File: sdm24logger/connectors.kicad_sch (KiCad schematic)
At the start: 23 parts, among them J3 USB_B, J4 1-776087-4, J5 1-776087-1, U10 SN65HVD230, U11 TLX9291A, U12 TCA9406DC, U13 ADC128D818, U8 USBLC6-2SC6, U9 SN65HVD230

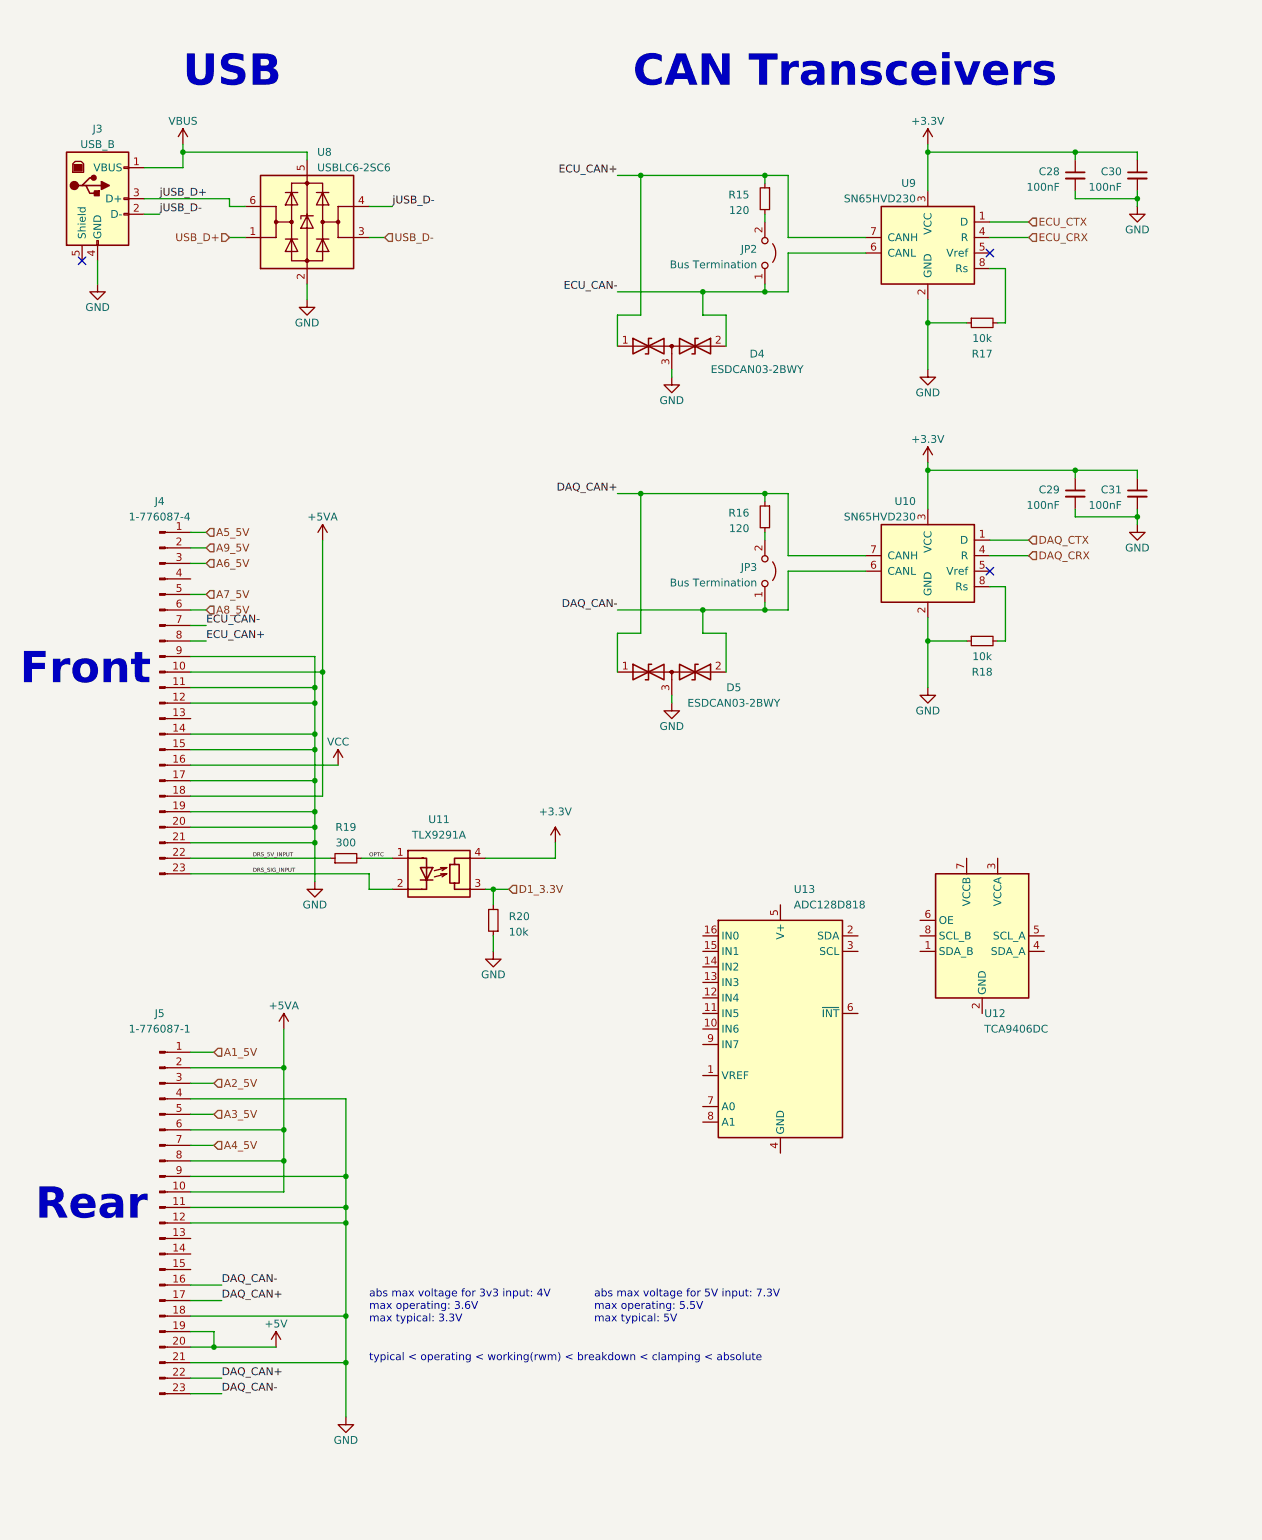
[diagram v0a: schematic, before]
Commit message: adding model for i2c shifter
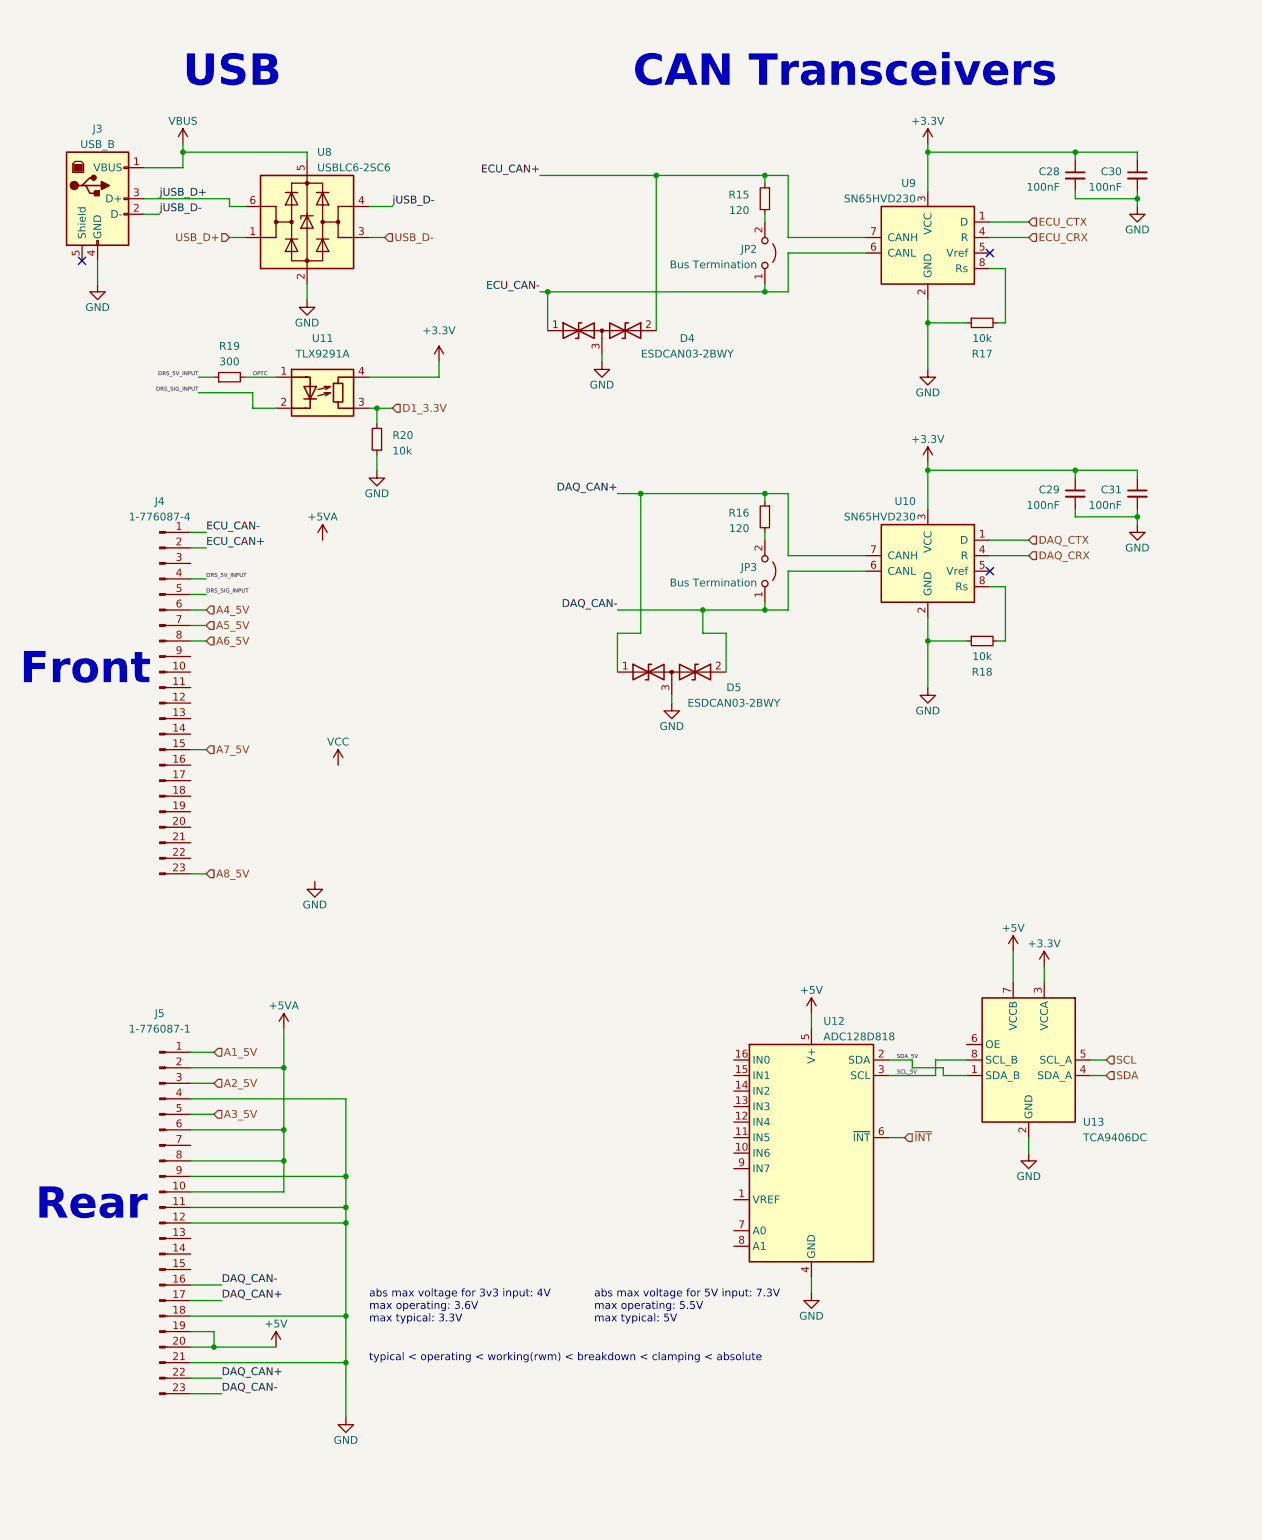
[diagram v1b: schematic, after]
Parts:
- U13: renamed from U12; footprint (none) -> Library:TI_SSOP_8_2.9x4.25x0.65
- renumbered U13 to U12
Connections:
- net A9_5V is gone; now on net ECU_CAN+: J4.2 (Pin_2)
- net +3.3V: now also U13.3 (VCCA)
- net +5V: now also U12.5 (V+), U13.7 (VCCB)
- net +5VA: no longer J4.10 (Pin_10), J4.18 (Pin_18)
- net A4_5V: now also J4.6 (Pin_6); no longer J5.7 (Pin_7)
- net A5_5V: now also J4.7 (Pin_7); no longer J4.1 (Pin_1)
- net A6_5V: now also J4.8 (Pin_8); no longer J4.3 (Pin_3)
- net A7_5V: now also J4.15 (Pin_15); no longer J4.5 (Pin_5)
- net A8_5V: now also J4.23 (Pin_23); no longer J4.6 (Pin_6)
- net DRS_5V_INPUT: now also J4.4 (Pin_4); no longer J4.22 (Pin_22)
- net DRS_SIG_INPUT: now also J4.5 (Pin_5); no longer J4.23 (Pin_23)
- net ECU_CAN+: now also D4.2 (A2); no longer D4.1 (A1), J4.8 (Pin_8)
- net ECU_CAN-: now also D4.1 (A1), J4.1 (Pin_1); no longer D4.2 (A2), J4.7 (Pin_7)
- net GND: now also U12.4 (GND), U13.2 (GND); no longer J4.11 (Pin_11), J4.12 (Pin_12), J4.14 (Pin_14), J4.15 (Pin_15), J4.17 (Pin_17), J4.19 (Pin_19), J4.20 (Pin_20), J4.21 (Pin_21), J4.9 (Pin_9)
- net VCC: no longer J4.16 (Pin_16)
- net SDA_5V: now reaches U13.1 (SDA_B)
- net SDA_5V: now also U12.2 (SDA)
- net SDA: now reaches U13.4 (SDA_A)
- net SCL: now reaches U13.5 (SCL_A)
- net SCL_5V: now reaches U13.8 (SCL_B)
- net SCL_5V: now also U12.3 (SCL)
- net ~{INT}: now reaches U12.6 (~{INT})
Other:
- moved on the sheet: D4, R19, R20, U11, U12, U13

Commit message: uploading
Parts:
- added C34, C35: 100nF, Capacitor_SMD:C_0402_1005Metric, symbol Device:C_Small
- added R21: 10k, Resistor_SMD:R_0603_1608Metric, symbol Device:R_Small
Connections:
- net +3.3V: now also C35.1
- net +5V: now also C34.1
- net +5VA: no longer J5.8 (Pin_8)
- net DAQ_CAN+: now also J5.7 (Pin_7); no longer J5.17 (Pin_17)
- net DAQ_CAN-: now also J5.8 (Pin_8); no longer J5.16 (Pin_16)
- net GND: now also C34.2, C35.2, R21.1; no longer J5.9 (Pin_9)
- net OE: now reaches U13.6 (OE)
- net OE: now also R21.2
- net A1_5V: no longer names the net of J5.1 (Pin_1)
- net A2_5V: no longer names the net of J5.3 (Pin_3)
- net A3_5V: no longer names the net of J5.5 (Pin_5)
- net A4_5V: no longer names the net of J4.6 (Pin_6)
- net A5_5V: no longer names the net of J4.7 (Pin_7)
- net A6_5V: no longer names the net of J4.8 (Pin_8)
- net A7_5V: no longer names the net of J4.15 (Pin_15)
- net A8_5V: no longer names the net of J4.23 (Pin_23)
- no-connect marks 3 -> 5
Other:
- moved on the sheet: U12

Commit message: ADC pinouts
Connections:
- net +5VA is gone; now on net +5V: J5.10 (Pin_10), J5.2 (Pin_2), J5.6 (Pin_6)
- net GND: now also U12.7 (A0), U12.8 (A1)
- net VCC: now also J4.16 (Pin_16)
- net AIN1: now reaches J4.15 (Pin_15)
- net AIN1: now also U12.12 (IN4)
- net AIN0: now reaches J4.23 (Pin_23)
- net AIN0: now also U12.13 (IN3)
- net AIN4: now reaches J4.6 (Pin_6)
- net AIN4: now also U12.9 (IN7)
- net AIN3: now reaches J4.7 (Pin_7)
- net AIN3: now also U12.10 (IN6)
- net AIN2: now reaches J4.8 (Pin_8)
- net AIN2: now also U12.11 (IN5)
- net AIN7: now reaches U12.14 (IN2)
- net AIN7: now also J5.16 (Pin_16)
- net AIN6: now reaches U12.15 (IN1)
- net AIN6: now also J5.9 (Pin_9)
- net AIN5: now reaches U12.16 (IN0)
- net AIN5: now also J5.1 (Pin_1)

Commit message: uploading changes
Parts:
- removed C34, C35: 100nF, Capacitor_SMD:C_0402_1005Metric, symbol Device:C_Small
- removed R21: 10k, Resistor_SMD:R_0603_1608Metric, symbol Device:R_Small
- removed U12: ADC128D818, Package_SO:TSSOP-16_4.4x5mm_P0.65mm, symbol Analog_ADC:ADC128D818
- removed U13: TCA9406DC, Library:TI_SSOP_8_2.9x4.25x0.65, symbol Interface:TCA9406DC
- added U12: ADR425ARMZ, Package_SO:MSOP-8_3x3mm_P0.65mm, symbol Reference_Voltage:ADR425ARMZ
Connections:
- net AIN0: now also J5.1 (Pin_1); no longer J4.23 (Pin_23)
- net AIN1: now also J5.9 (Pin_9); no longer J4.15 (Pin_15)
- net AIN2: now also J5.16 (Pin_16); no longer J4.8 (Pin_8)
- net AIN3: now also J4.23 (Pin_23); no longer J4.7 (Pin_7)
- net AIN4: now also J4.15 (Pin_15); no longer J4.6 (Pin_6)
- net AIN5: now also J4.8 (Pin_8); no longer J5.1 (Pin_1)
- net AIN6: now also J4.7 (Pin_7); no longer J5.9 (Pin_9)
- net AIN7: now also J4.6 (Pin_6); no longer J5.16 (Pin_16)
- net GND: now also U12.4 (GND)
- net VCC: now also U12.2 (VIN)
- new net +5VA: U12.6 (OUT)
- no-connect marks 5 -> 6

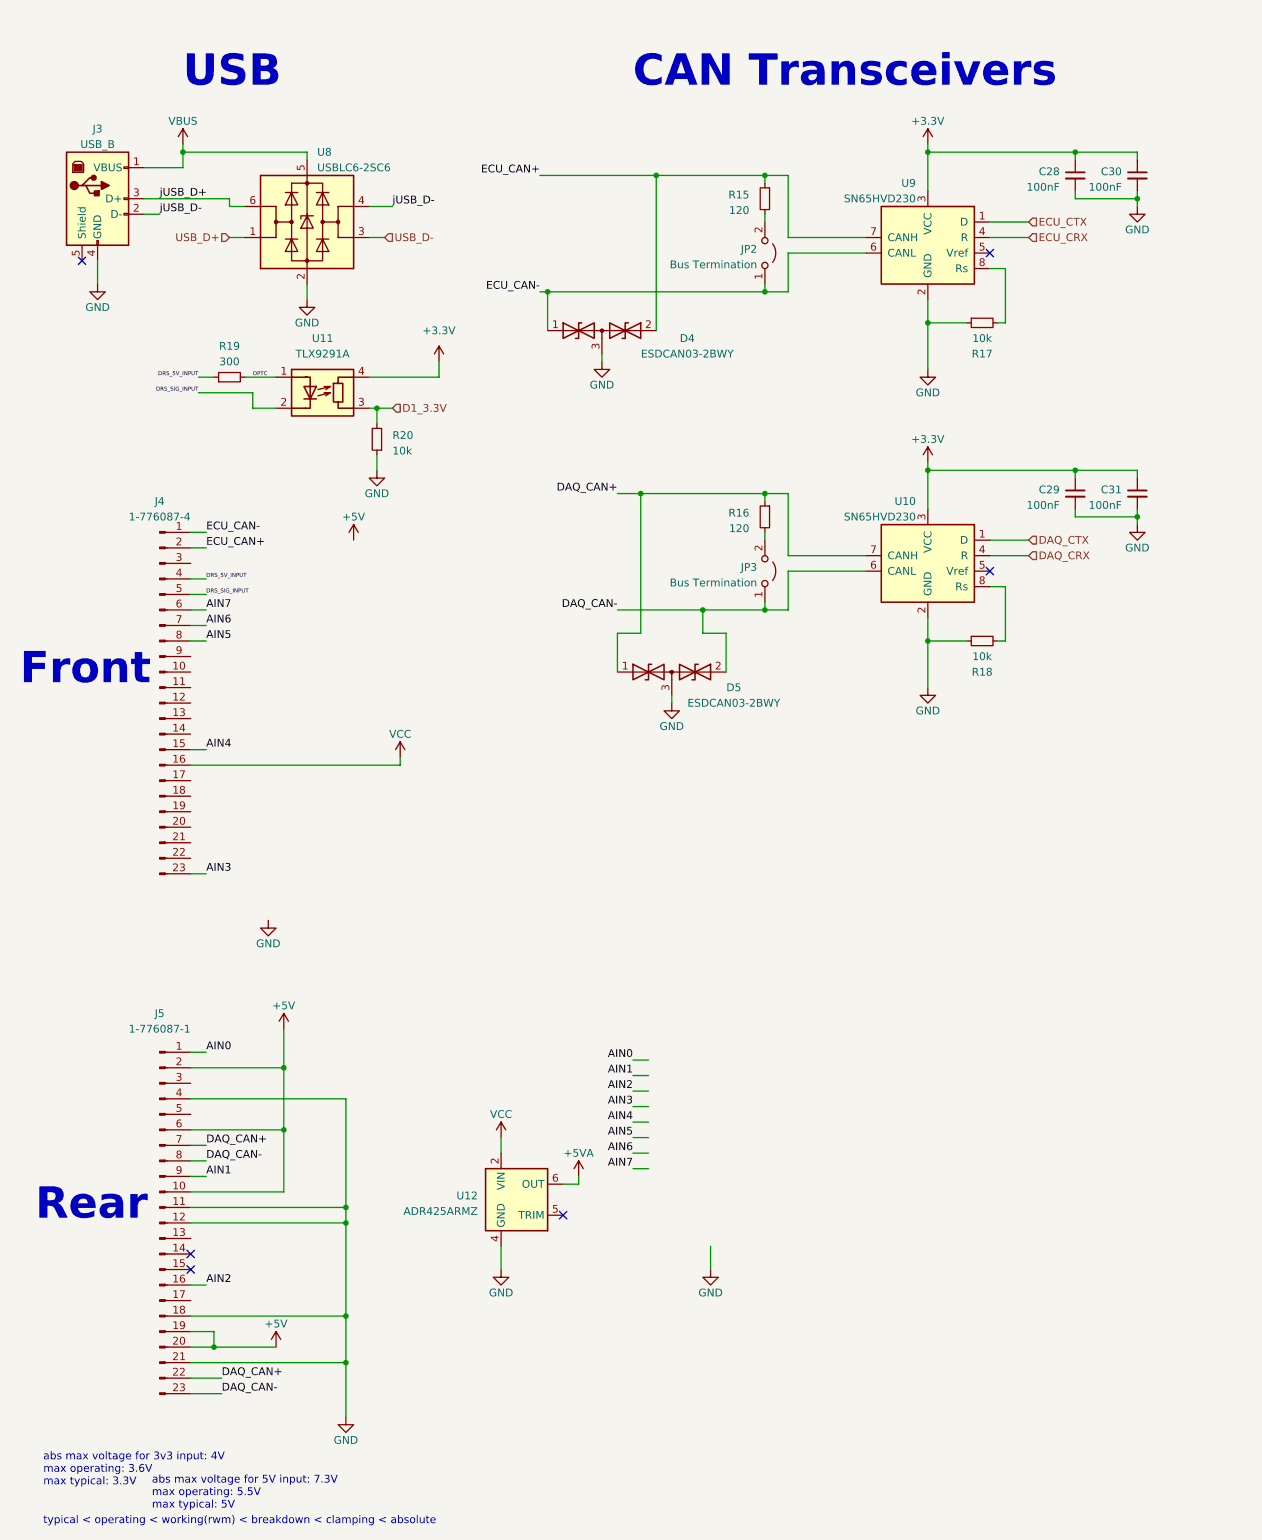
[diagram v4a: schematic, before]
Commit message: add footprints for volt ref
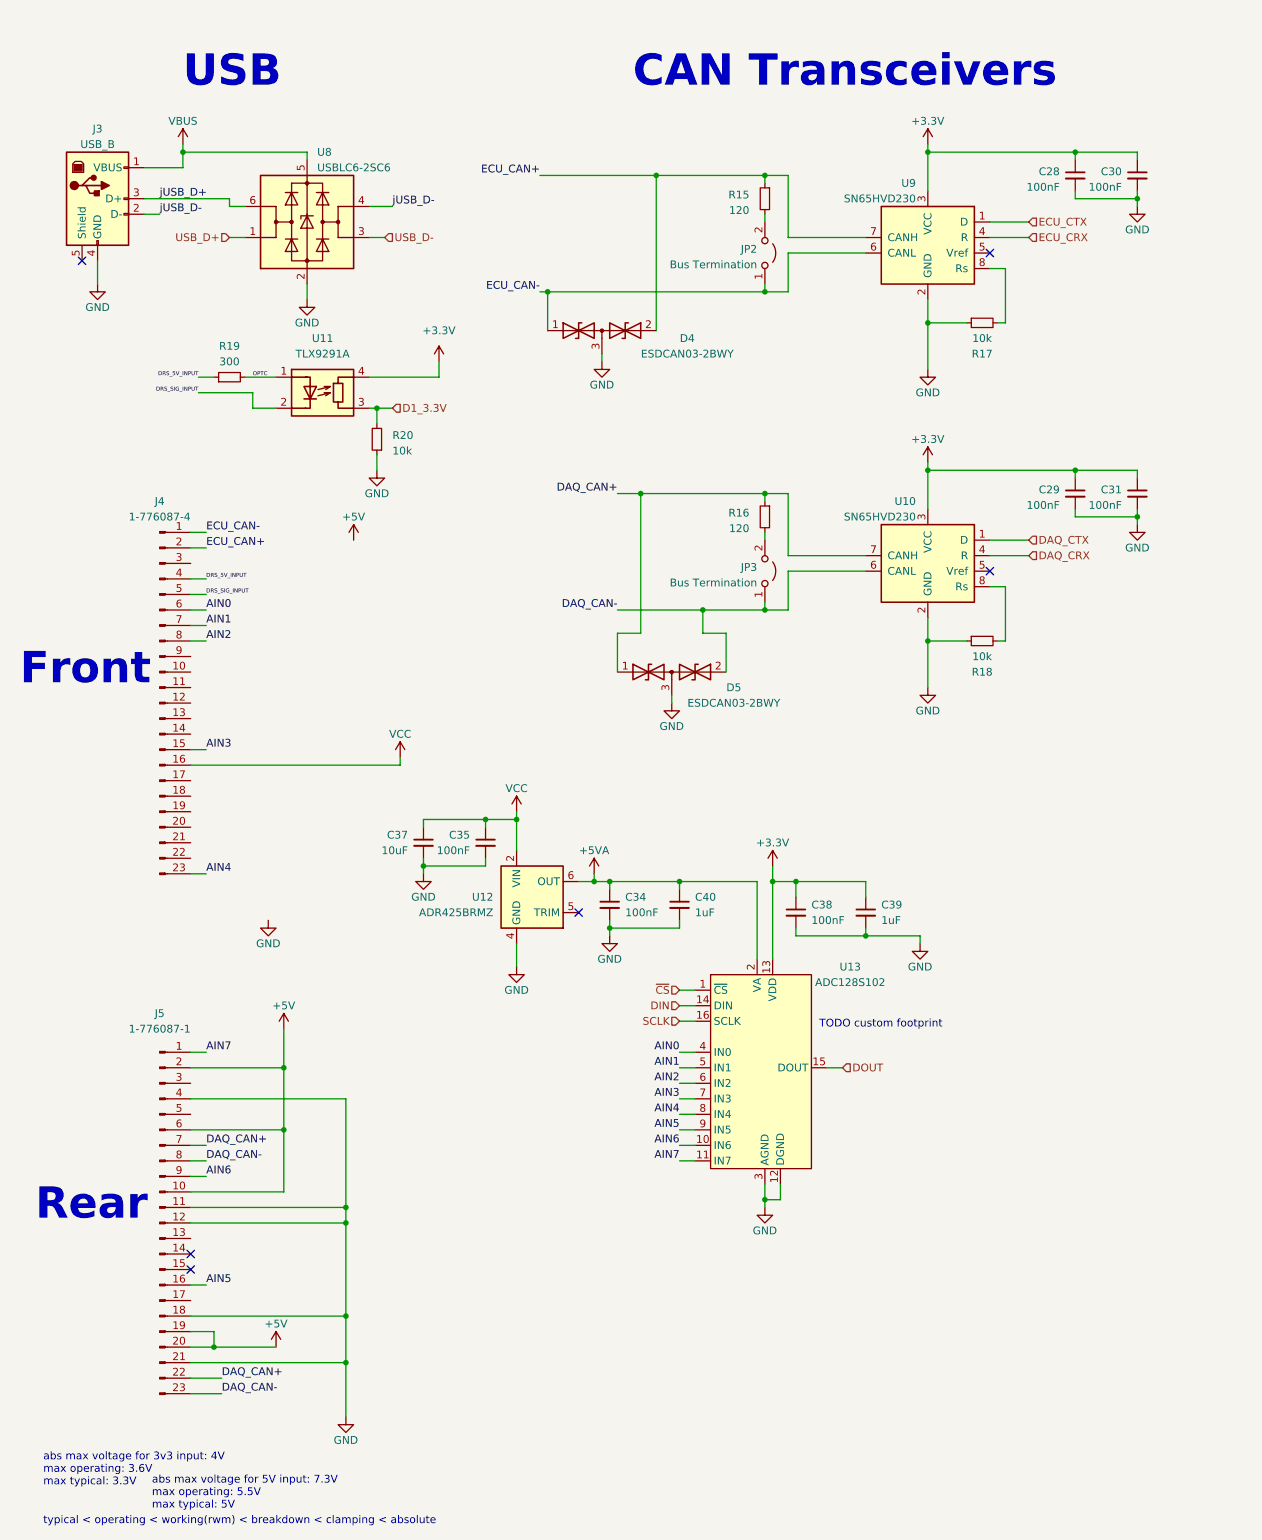
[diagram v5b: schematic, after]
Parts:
- added C34, C35, C38: 100nF, Capacitor_SMD:C_0402_1005Metric, symbol Device:C_Small
- added C37: 10uF, Capacitor_SMD:C_0805_2012Metric, symbol Device:C_Small
- added C39, C40: 1uF, Capacitor_SMD:C_0603_1608Metric, symbol Device:C_Small
- added U13: ADC128S102, Package_SO:TSSOP-16_4.4x5mm_P0.65mm, symbol lib:TI_ADC128S102
- U12: value ADR425ARMZ -> ADR425BRMZ
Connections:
- net +3.3V: now also C38.1, C39.1, U13.13 (VDD)
- net +5VA: now also C34.1, C40.1, U13.2 (VA)
- net AIN0: now also J4.6 (Pin_6), U13.4 (IN0); no longer J5.1 (Pin_1)
- net AIN1: now also J4.7 (Pin_7), U13.5 (IN1); no longer J5.9 (Pin_9)
- net AIN2: now also J4.8 (Pin_8), U13.6 (IN2); no longer J5.16 (Pin_16)
- net AIN3: now also J4.15 (Pin_15), U13.7 (IN3); no longer J4.23 (Pin_23)
- net AIN4: now also J4.23 (Pin_23), U13.8 (IN4); no longer J4.15 (Pin_15)
- net AIN5: now also J5.16 (Pin_16), U13.9 (IN5); no longer J4.8 (Pin_8)
- net AIN6: now also J5.9 (Pin_9), U13.10 (IN6); no longer J4.7 (Pin_7)
- net AIN7: now also J5.1 (Pin_1), U13.11 (IN7); no longer J4.6 (Pin_6)
- net GND: now also C34.2, C35.2, C37.2, C38.2, C39.2, C40.2, U13.12 (DGND), U13.3 (AGND)
- net VCC: now also C35.1, C37.1
- new net DIN: U13.14 (DIN)
- new net DOUT: U13.15 (DOUT)
- new net SCLK: U13.16 (SCLK)
- new net ~{CS}: U13.1 (~{CS})
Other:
- note added: "TODO custom footprint"
- moved on the sheet: U12

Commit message: start routing on logger
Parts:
- renumbered C37 to C31, C35 to C32, C34 to C33, C40 to C34, C38 to C35, C39 to C36, C28 to C37, C29 to C38, C30 to C39, C31 to C40, R19 to R16, R20 to R17, R15 to R18, R16 to R19, R17 to R20, R18 to R21, U12 to U10, U13 to U11, U9 to U12, U10 to U13, U11 to U9
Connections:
- net +5V: now also J4.12 (Pin_12), J4.13 (Pin_13), J4.19 (Pin_19), J4.20 (Pin_20), J4.21 (Pin_21), J5.13 (Pin_13), J5.17 (Pin_17), J5.18 (Pin_18); no longer J5.10 (Pin_10), J5.2 (Pin_2), J5.6 (Pin_6)
- net DAQ_CAN+: now also D5.2 (A2), J5.23 (Pin_23), J5.8 (Pin_8); no longer D5.1 (A1), J5.22 (Pin_22), J5.7 (Pin_7)
- net DAQ_CAN-: now also D5.1 (A1), J5.22 (Pin_22), J5.7 (Pin_7); no longer D5.2 (A2), J5.23 (Pin_23), J5.8 (Pin_8)
- net GND: now also J4.10 (Pin_10), J4.11 (Pin_11), J4.14 (Pin_14), J4.17 (Pin_17), J4.22 (Pin_22), J4.9 (Pin_9), J5.2 (Pin_2), J5.6 (Pin_6); no longer J5.18 (Pin_18), J5.4 (Pin_4)
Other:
- note added: "8-Channel ADC"
- note added: "Opto- coupler"
- moved on the sheet: C31, C32, C33, C34, C35, C36, U10, U11
